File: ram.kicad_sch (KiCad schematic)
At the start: 25 parts, among them U16 XX4256, U17 XX4256, U18 XX4256, U19 XX4256, U20 XX4256, U21 XX4256, U22 XX4256, U23 XX4256, U32 74LS139, U34 74LS373, U35 74LS244

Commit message: DRAM chips replaced with SIMM module
Added logic to decode 2MB chip + 1.5MB slow
Rewired trapdoor slot
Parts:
- removed JP3A1, JP3B1: Jumper_2_Bridged, Raemixx500:Jumper2-Bridged, symbol Jumper:Jumper_2_Bridged
- removed JP4A1, JP4B1: Jumper_3_Open, Raemixx500:Jumper3-Open, symbol Jumper:Jumper_3_Open
- removed U16, U17, U18, U19, U20, U21, U22, U23: XX4256, Package_DIP:DIP-20_W7.62mm_Socket_LongPads, symbol XX4256:XX4256
- added JP201: Jumper_3_Bridged23, Raemixx500:Jumper3-Bridged23, symbol Jumper_3_Bridged23:Jumper_3_Bridged23
- added R203, R204, R205: 4.7k, Raemixx500:R_Axial_DIN0309_L9.0mm_D3.2mm_P12.70mm_Horizontal, symbol Device:R
- added R206, R207, R208: 68, Raemixx500:R_Axial_DIN0309_L9.0mm_D3.2mm_P12.70mm_Horizontal, symbol Device:R
- added U16: SIMM, Raemixx500:SIMM_TE_Connectivity_5822134-3, symbol Raemixx:SIMM module 72pins
- added U17: 74LS08, Package_DIP:DIP-14_W7.62mm_Socket_LongPads, symbol 74xx:74LS08
- added U18: 74LS74, Package_DIP:DIP-14_W7.62mm_Socket_LongPads, symbol 74xx:74LS74
- added U19: 74LS00, Package_DIP:DIP-14_W7.62mm_Socket_LongPads, symbol 74xx:74LS00
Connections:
- net ~{BRAS0} is gone; now on net ~{BCASU1}: RP203.1 (R1.1)
- net GND: now also U35.2 (I0a), U35.4 (I1a), U35.6 (I2a), U35.8 (I3a), JP201.3 (B), U16.1 (VSS), U16.19 (A10), U16.29 (A11), U16.39 (VSS), U16.72 (VSS), U17.7 (GND), U18.10 (~{S}), U18.11 (C), U18.12 (D), U18.13 (~{R}), U18.7 (GND), U19.7 (GND)
- net VCC: now also R203.2, R204.1, R205.2, U16.10 (VCC), U16.30 (VCC), U16.59 (VCC), U17.14 (VCC), U18.1 (~{R}), U18.14 (VCC), U18.4 (~{S}), U19.14 (VCC)
- net bdra9: now also RP201.2 (R1.2); no longer U32.14 (A0), U32.2 (A0)
- net ~{BCASL1}: now also RP203.5 (R3.1), U16.41 (~{CAS2}); no longer U32.5 (O1)
- net ~{BCASU1}: now also U16.42 (~{CAS3}); no longer U32.11 (O1)
- net ~{BWE}: now also RP203.10 (R5.2), U16.47 (~{WE}); no longer RP203.9 (R5.1), U35.3 (O3b)
- net ~{CASL}: now also U32.1 (E); no longer U32.3 (A1), U35.6 (I2a)
- net ~{CASU}: now also U32.15 (E); no longer U32.13 (A1), U35.8 (I3a)
- net ~{RAS0}: now also U17.13; no longer U35.2 (I0a)
- net ~{RAS1}: now also U17.12; no longer U35.4 (I1a)
- net at U34.11 (LE), U35.5 (O2b): no longer U32.1 (E), U32.15 (E)
- net at U32.7 (O3): now also R207.1
- net at U32.9 (O3): now also R208.1
- net at RP203.8 (R4.2): now also U32.4 (O0)
- net at RP203.2 (R1.2): now also U32.11 (O1); no longer R201.2
- net at RP203.6 (R3.2): now also U32.5 (O1)
- net at RP203.4 (R2.2): now also U32.12 (O0); no longer R202.2
- net MA9: now reaches RP201.1 (R1.1)
- net MA9: now also U16.32 (A9)
- net ma0 renamed MA0
- net MA0: now also U16.12 (A0)
- net ma1 renamed MA1
- net MA1: now also U16.13 (A1)
- net ma2 renamed MA2
- net MA2: now also U16.14 (A2)
- net ma3 renamed MA3
- net MA3: now also U16.15 (A3)
- net ma4 renamed MA4
- net MA4: now also U16.16 (A4)
- net ma5 renamed MA5
- net MA5: now also U16.17 (A5)
- net ma6 renamed MA6
- net MA6: now also U16.18 (A6)
- net ma7 renamed MA7
- net MA7: now also U16.28 (A7)
- net ma8 renamed MA8
- net MA8: now also U16.31 (A8)
- net ~{BRAS1} renamed ~{BCASU0}
- net ~{BCASU0}: now also U16.43 (~{CAS1})
- net ~{bcasl0} renamed ~{BCASL0}
- net ~{BCASL0}: now also U16.40 (~{CAS0}); no longer U32.4 (O0)
- removed net ~{bcasu0}: RP203.5 (R3.1), U32.12 (O0)
- new net: JP201.2 (C), U32.14 (A0), U32.2 (A0)
- new net: R201.2, U16.37 (PDQ2)
- new net: R202.2, U16.35 (PDQ3)
- new net: RP203.9 (R5.1), U35.3 (O3b)
- new net: U19.1, U19.10, U19.11
- new net: U17.6, U19.2
- new net: U17.3, U17.4, U19.4
- new net: R206.1, U17.11
- new net: R203.1, U16.38 (PDQ4)
- new net: U17.8, U18.2 (D)
- new net: R205.1, U16.33 (~{RAS3}), U16.45 (~{RAS1})
- new net: U19.6, U19.9
- new net: R204.2, U16.36 (PDQ1)
- new net A19: U17.1
- new net A20: U17.2
- new net A22: U17.5, U19.5
- new net A23: U17.9
- new net CCKQ: U18.3 (C)
- new net DRD0: U16.2 (DQ1), U16.3 (DQ17)
- new net DRD1: U16.4 (DQ2), U16.5 (DQ18)
- new net DRD10: U16.53 (DQ11), U16.54 (DQ27)
- new net DRD11: U16.55 (DQ12), U16.56 (DQ28)
- new net DRD12: U16.57 (DQ13), U16.58 (DQ29)
- new net DRD13: U16.60 (DQ30), U16.61 (DQ14)
- new net DRD14: U16.62 (DQ31), U16.63 (DQ15)
- new net DRD15: U16.64 (DQ32), U16.65 (DQ16)
- new net DRD2: U16.6 (DQ3), U16.7 (DQ19)
- new net DRD3: U16.8 (DQ4), U16.9 (DQ20)
- new net DRD4: U16.20 (DQ5), U16.21 (DQ21)
- new net DRD5: U16.22 (DQ6), U16.23 (DQ22)
- new net DRD6: U16.24 (DQ7), U16.25 (DQ23)
- new net DRD7: U16.26 (DQ8), U16.27 (DQ24)
- new net DRD8: U16.49 (DQ9), U16.50 (DQ25)
- new net DRD9: U16.51 (DQ10), U16.52 (DQ26)
- new net SEL_SLOW: JP201.1 (A), U18.5 (Q), U32.13 (A1), U32.3 (A1)
- new net ~{BCASL3}: R207.2
- new net ~{BCASU3}: R208.2
- new net ~{BLIT}: U17.10
- new net ~{BRAS}: R206.2, U16.34 (~{RAS2}), U16.44 (~{RAS0})
- new net ~{RAMEN_GARY}: U19.12
- new net ~{RAMEN}: U19.8
- new net ~{REGEN_GARY}: U19.13
- new net ~{REGEN}: U19.3
- no-connect marks 6 -> 13
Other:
- note removed: "A600 has a KLUDGE here with a 74LS00. Is it needed here too?"
- note removed: "JP3 swaps upper and lower RAM banks"
- note removed: "Note: JP4 bypasses U32 for 512K system"
- note removed: "Note: U20-23, U32 not loaded for 512K system Required chips are 256k×4. For a list of compatible RAM chips see: https://www.amiga-stuff.com/hardware/256kx4-dram.html"
- note removed: "bdra9 does not pass through RP because it does not get to RAMs. But there's a spare resistor in case."
- title: Rämixx500 -> Rämixx500_max
- moved on the sheet: C16, C17, C18, C19, C20, R201, R202, RP201, RP202, RP203, U32A, U32B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

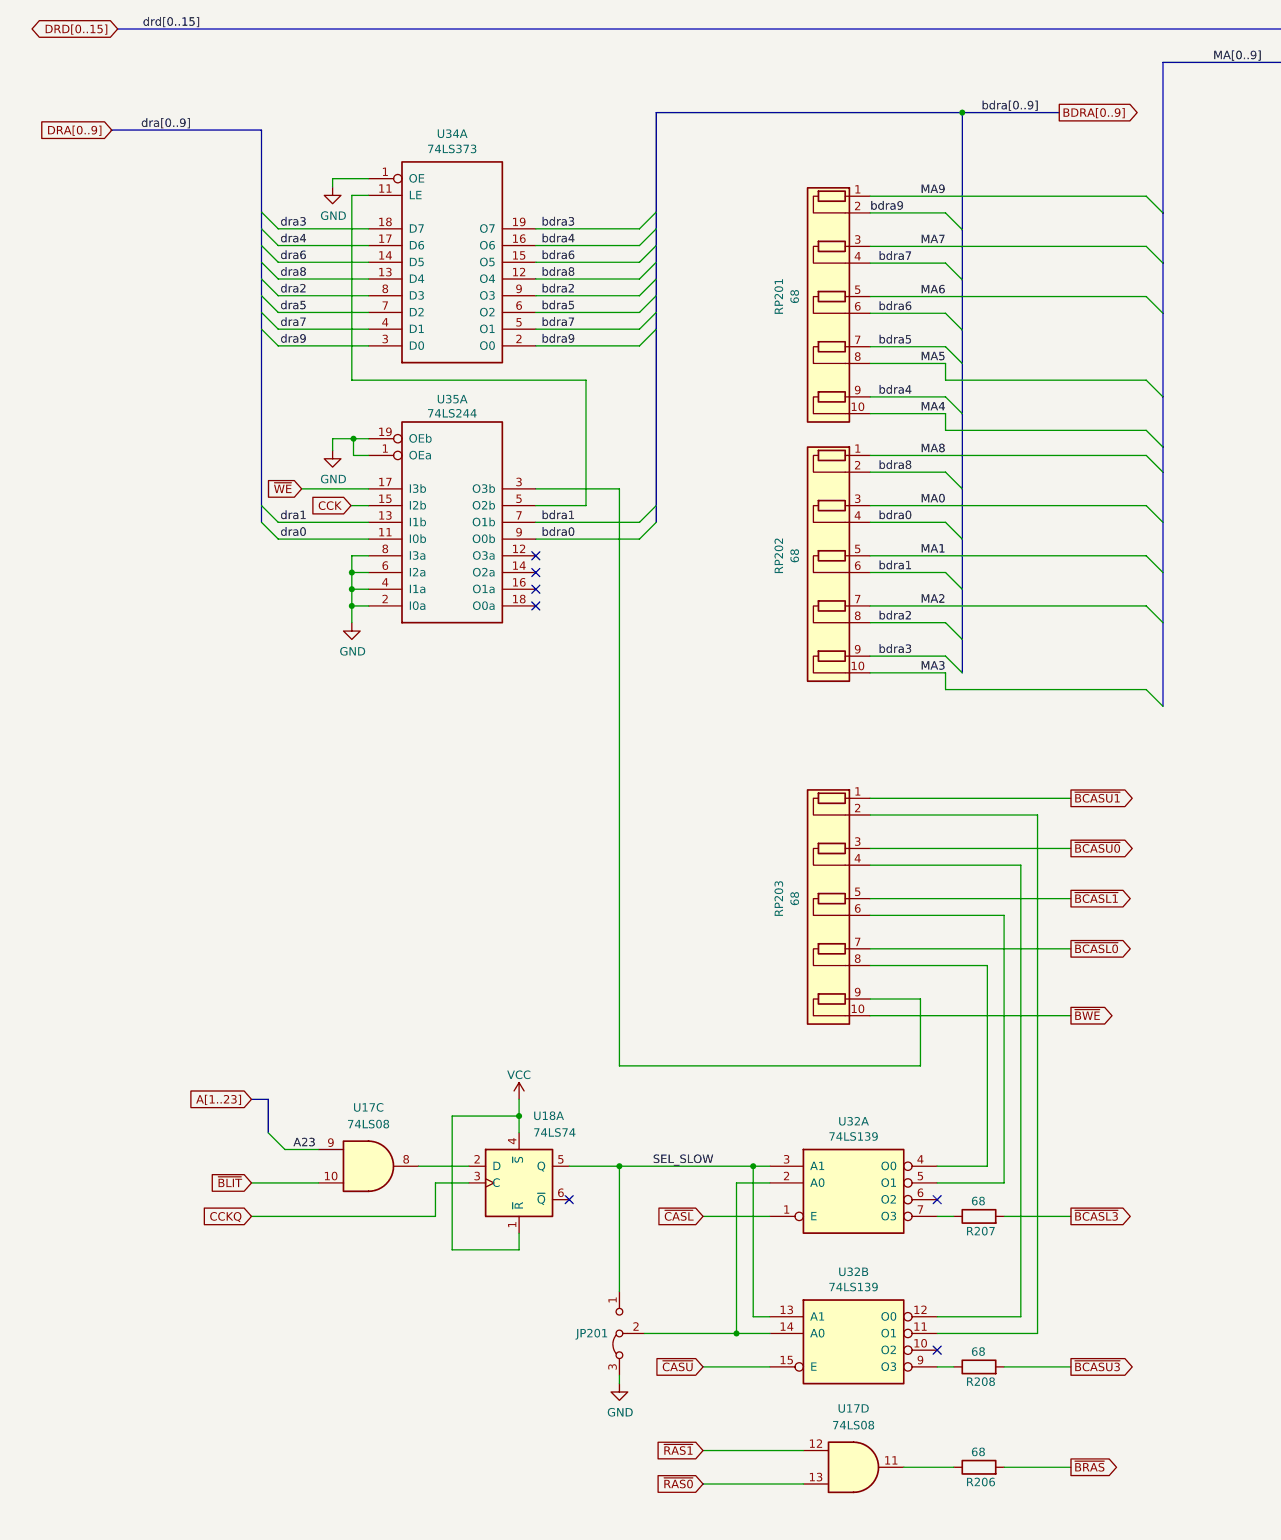
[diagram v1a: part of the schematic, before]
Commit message: optimized timing
removed CCK from RAM buffers to ease routing
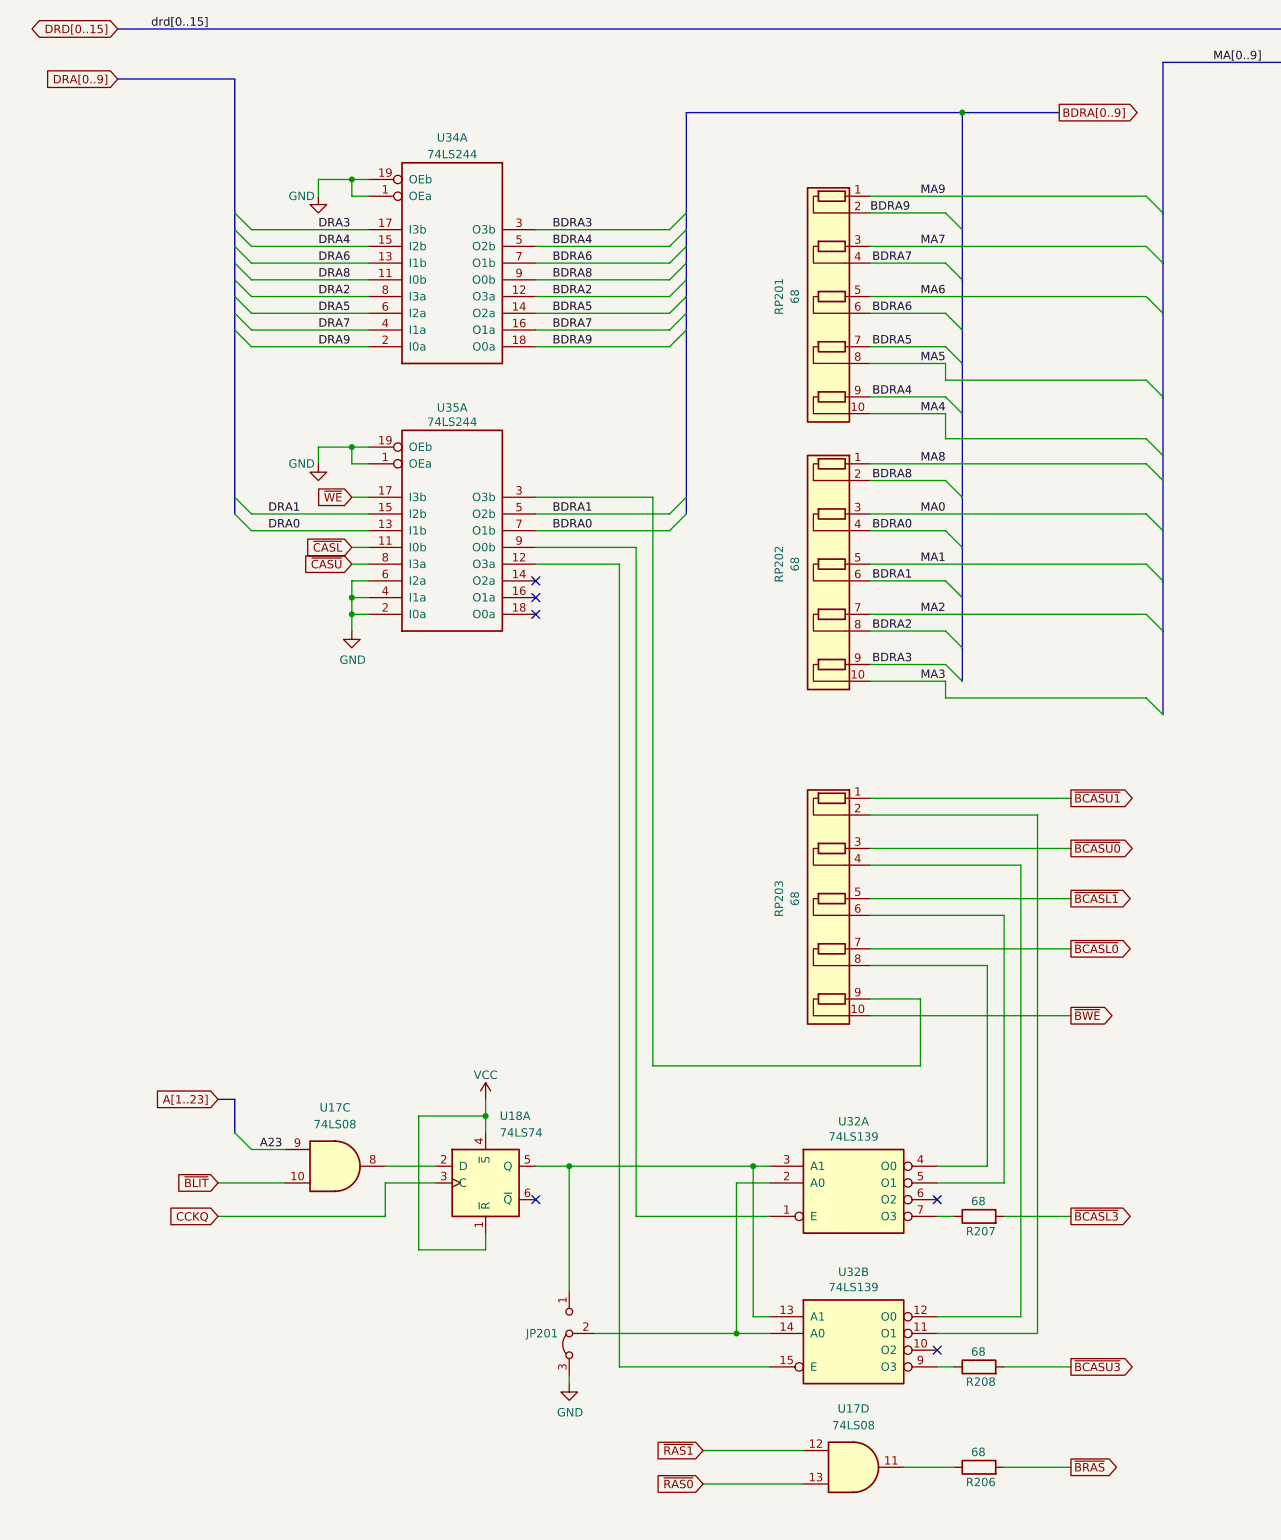
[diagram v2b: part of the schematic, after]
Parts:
- removed U34: 74LS373, Package_DIP:DIP-20_W7.62mm_Socket_LongPads, symbol 74ls373:74LS373
- added U34: 74LS244, symbol 74ls244:74LS244
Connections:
- net dra0 is gone; now on net ~{CASL}: U35.11 (I0b)
- net GND: now also U34.1 (OEa), U34.19 (OEb); no longer U35.8 (I3a)
- net ~{CASL}: no longer U32.1 (E)
- net ~{CASU}: now also U35.8 (I3a); no longer U32.15 (E)
- net BDRA1: now reaches U35.5 (O2b)
- net BDRA1: now also RP202.6 (R3.2)
- net at U35.12 (O3a): now also U32.15 (E)
- net CCK renamed DRA1
- net SEL_SLOW: no longer names the net of JP201.1 (A), U18.5 (Q), U32.13 (A1), U32.3 (A1)
- net bdra0: no longer names the net of U35.9 (O0b)
- net bdra0: now also U32.1 (E); no longer RP202.4 (R2.2)
- net bdra1 renamed BDRA0
- net BDRA0: now also RP202.4 (R2.2); no longer RP202.6 (R3.2)
- net bdra2 renamed BDRA2
- net BDRA2: now also U34.12 (O3a)
- net bdra3 renamed BDRA3
- net BDRA3: now also U34.3 (O3b)
- net bdra4 renamed BDRA4
- net BDRA4: now also U34.5 (O2b)
- net bdra5 renamed BDRA5
- net BDRA5: now also U34.14 (O2a)
- net bdra6 renamed BDRA6
- net BDRA6: now also U34.7 (O1b)
- net bdra7 renamed BDRA7
- net BDRA7: now also U34.16 (O1a)
- net bdra8 renamed BDRA8
- net BDRA8: now also U34.9 (O0b)
- net bdra9 renamed BDRA9
- net BDRA9: now also U34.18 (O0a)
- net dra1 renamed DRA0
- new net DRA2: U34.8 (I3a)
- new net DRA3: U34.17 (I3b)
- new net DRA4: U34.15 (I2b)
- new net DRA5: U34.6 (I2a)
- new net DRA6: U34.13 (I1b)
- new net DRA7: U34.4 (I1a)
- new net DRA8: U34.11 (I0b)
- new net DRA9: U34.2 (I0a)
- no-connect marks 13 -> 12
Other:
- moved on the sheet: JP201, RP202, U17C, U18A, U35A

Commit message: removed JP2
some more small fixes
schematic is now more or less done I think
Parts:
- added R209, R210: 68, Raemixx500:R_Axial_DIN0309_L9.0mm_D3.2mm_P12.70mm_Horizontal, symbol Device:R
- U19: value 74LS00 -> 74F00
- U34: footprint (none) -> Package_DIP:DIP-20_W7.62mm_Socket_LongPads
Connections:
- net GND: no longer U35.6 (I2a)
- net ~{RAMEN}: now also R209.2; no longer U19.8
- net ~{REGEN}: now also R210.2; no longer U19.3
- net at U35.14 (O2a): now also R206.1
- net at U17.11: now also U35.6 (I2a); no longer R206.1
- new net: R210.1, U19.3
- new net: R209.1, U19.8
- no-connect marks 12 -> 11
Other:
- note added: "SIMM must be at least 4MEG"
- note added: "slow RAM select 1-2 trapdoor 2-3 SIMM (default)"
- moved on the sheet: R206, R207, R208, RP203, U17D
